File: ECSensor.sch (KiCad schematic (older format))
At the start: 8 parts, among them J2 EC_Sensor_Input_3_Pin, Q2 Q_PMOS_DSG

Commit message: schematic and pcb redesign
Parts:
- added FB3, FB4, FB5: Ferrite_Bead, Inductor_SMD:L_0402_1005Metric, symbol Device:Ferrite_Bead
- added R16, R17, R18: 0, Resistor_SMD:R_0402_1005Metric, symbol Device:R_Small_US
- C33: renamed from C26; footprint Capacitor_SMD:C_0603_1608Metric -> Capacitor_SMD:C_0402_1005Metric
- C34: renamed from C27; footprint Capacitor_SMD:C_0603_1608Metric -> Capacitor_SMD:C_0402_1005Metric
- C35: renamed from C28; footprint Capacitor_SMD:C_0603_1608Metric -> Capacitor_SMD:C_0402_1005Metric
- R13: renamed from R7; footprint Resistor_SMD:R_0603_1608Metric -> Resistor_SMD:R_0402_1005Metric
- R14: renamed from R8; footprint Resistor_SMD:R_0603_1608Metric -> Resistor_SMD:R_0402_1005Metric
- R15: renamed from R9; footprint Resistor_SMD:R_0603_1608Metric -> Resistor_SMD:R_0402_1005Metric
- renumbered J2 to J3
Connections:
- net CE: now also FB3.2, R16.2; no longer J3.1 (Pin_1)
- net RE: now also FB5.2, R18.2; no longer J3.3 (Pin_3)
- net WE: now also FB4.2, R17.2; no longer J3.2 (Pin_2)
- new net: FB3.1, J3.1 (Pin_1), R16.1
- new net: FB4.1, J3.2 (Pin_2), R17.1
- new net: FB5.1, J3.3 (Pin_3), R18.1
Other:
- moved on the sheet: C36, C37, C38, J4

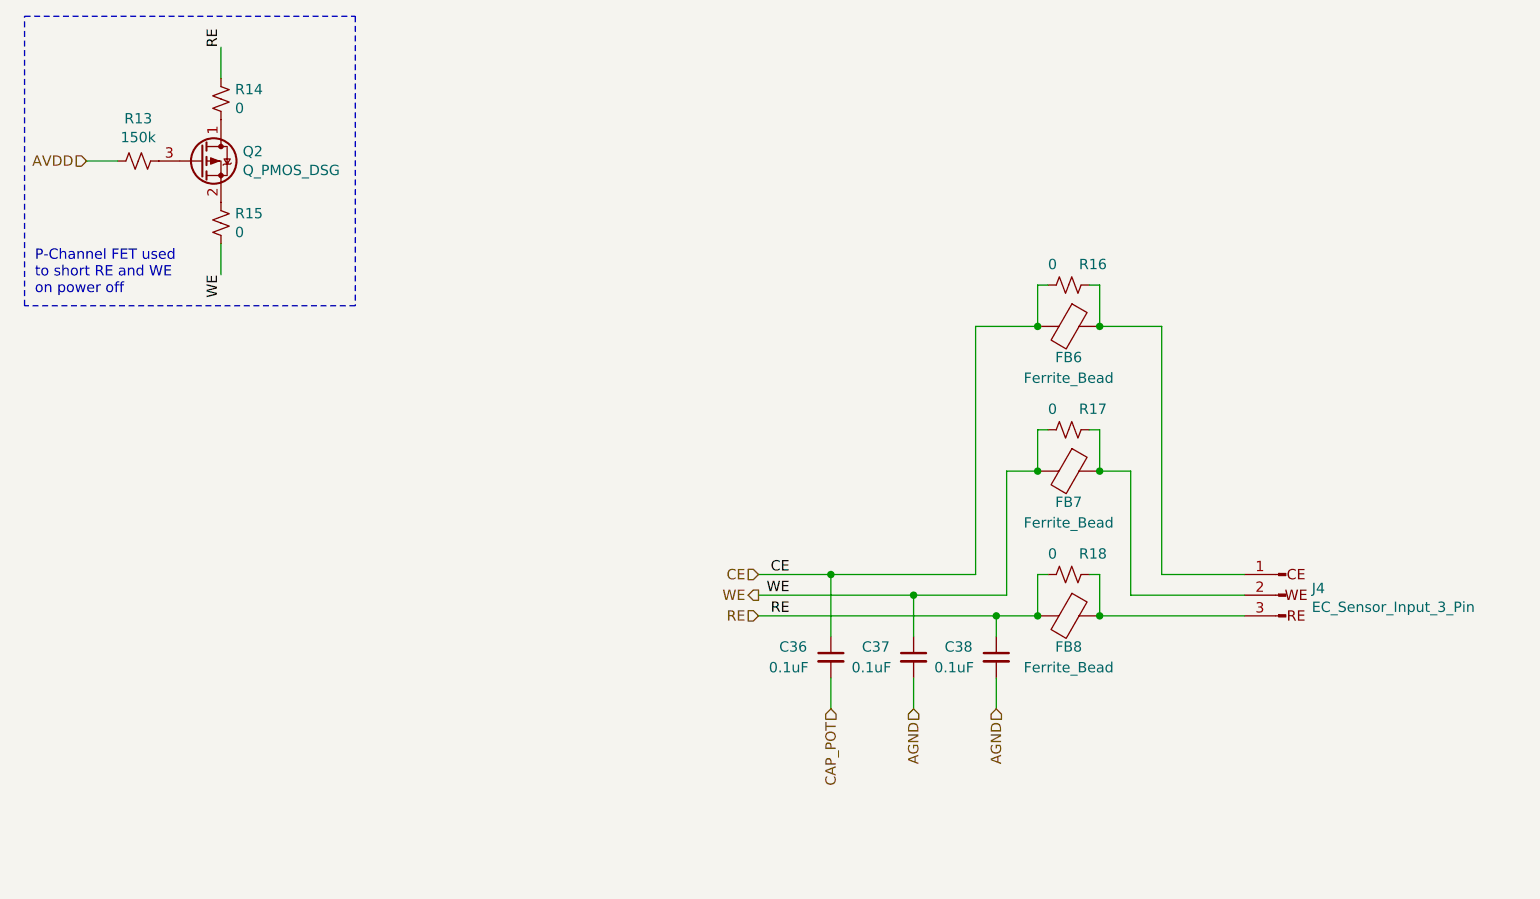
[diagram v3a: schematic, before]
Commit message: finsihed traces for one EC sensor
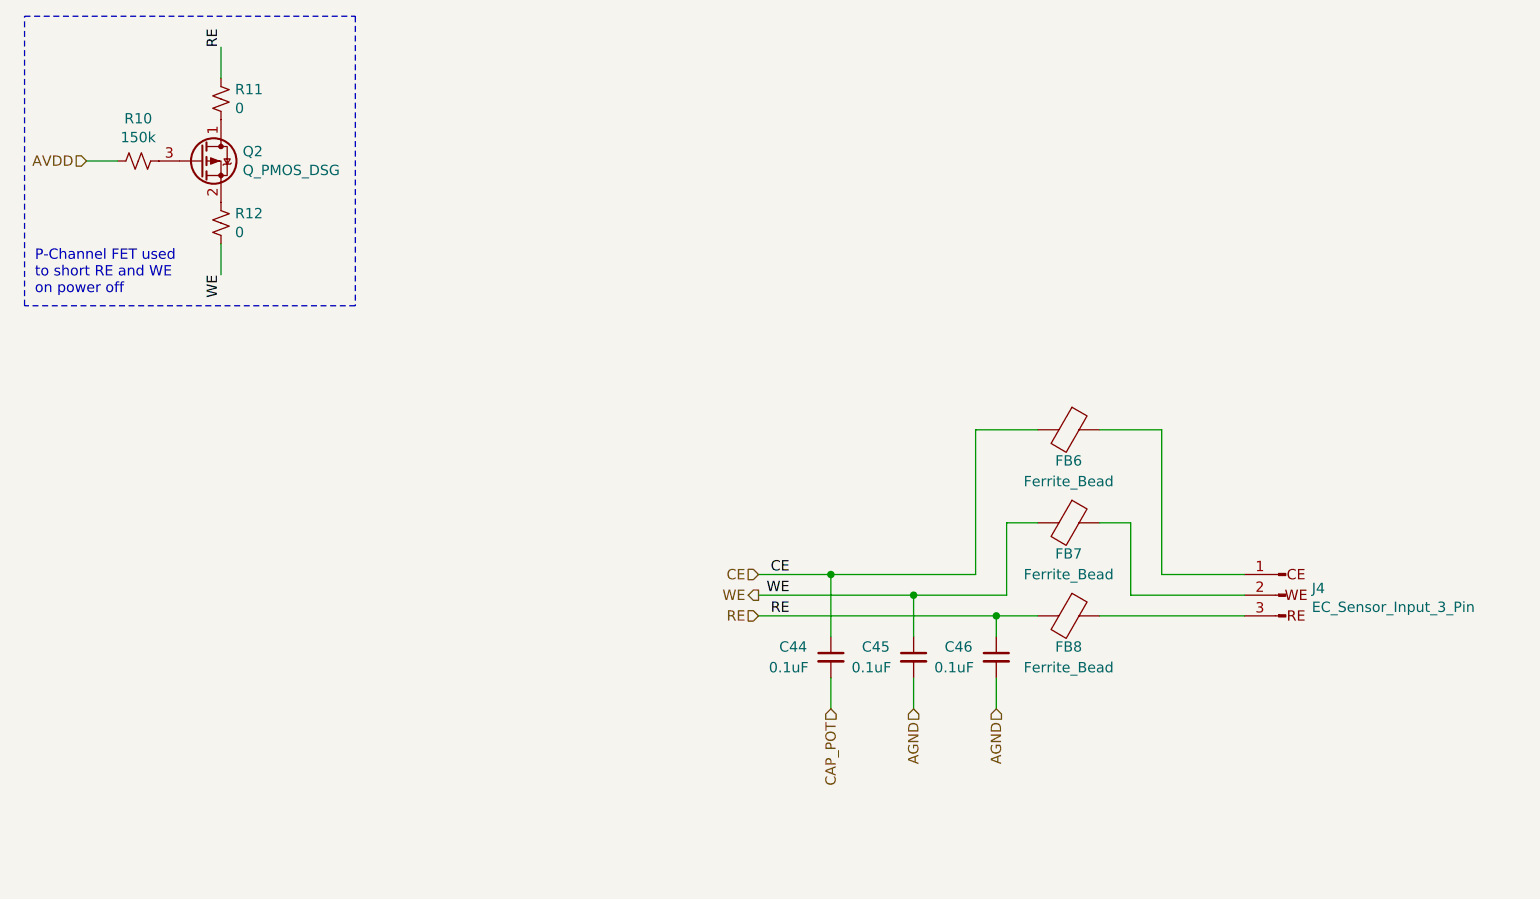
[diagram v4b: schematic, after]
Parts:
- removed R16, R17, R18: 0, Resistor_SMD:R_0402_1005Metric, symbol Device:R_Small_US
- renumbered C33 to C44, C34 to C45, C35 to C46, FB3 to FB6, FB4 to FB7, FB5 to FB8, J3 to J4, Q2 to Q1, R13 to R7, R14 to R8, R15 to R9
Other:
- moved on the sheet: FB6, FB7
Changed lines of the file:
@@
 $Descr A4 11693 8268
 encoding utf-8
-Sheet 2 5
+Sheet 5 5
 Title "ADuCM355 Template"
 Date ""
@@
 $EndDescr
 $Comp
-L Device:C_Small C34
+L Device:C_Small C45
 U 1 1 5DF76279
 P 5000 3750
-AR Path="/5DF7340A/5DF76279" Ref="C34"  Part="1"
-AR Path="/5DF54D0C/5DF76279" Ref="C37"  Part="1"
-F 0 "C37" H 4750 3800 50  0000 L CNN
+AR Path="/5DF7340A/5DF76279" Ref="C45"  Part="1"
+AR Path="/5DF54D0C/5DF76279" Ref="C34"  Part="1"
+F 0 "C45" H 4750 3800 50  0000 L CNN
 F 1 "0.1uF" H 4700 3700 50  0000 L CNN
 F 2 "Capacitor_SMD:C_0402_1005Metric" H 5000 3750 50  0001 C CNN
@@
 $EndComp
 $Comp
-L Device:C_Small C33
+L Device:C_Small C44
 U 1 1 5DF76497
 P 4600 3750
-AR Path="/5DF7340A/5DF76497" Ref="C33"  Part="1"
-AR Path="/5DF54D0C/5DF76497" Ref="C36"  Part="1"
-F 0 "C36" H 4350 3800 50  0000 L CNN
+AR Path="/5DF7340A/5DF76497" Ref="C44"  Part="1"
+AR Path="/5DF54D0C/5DF76497" Ref="C33"  Part="1"
+F 0 "C44" H 4350 3800 50  0000 L CNN
 F 1 "0.1uF" H 4300 3700 50  0000 L CNN
 F 2 "Capacitor_SMD:C_0402_1005Metric" H 4600 3750 50  0001 C CNN
@@
 $EndComp
 $Comp
-L Device:C_Small C35
+L Device:C_Small C46
 U 1 1 5DF768A0
 P 5400 3750
-AR Path="/5DF7340A/5DF768A0" Ref="C35"  Part="1"
-AR Path="/5DF54D0C/5DF768A0" Ref="C38"  Part="1"
-F 0 "C38" H 5150 3800 50  0000 L CNN
+AR Path="/5DF7340A/5DF768A0" Ref="C46"  Part="1"
+AR Path="/5DF54D0C/5DF768A0" Ref="C35"  Part="1"
+F 0 "C46" H 5150 3800 50  0000 L CNN
 F 1 "0.1uF" H 5100 3700 50  0000 L CNN
 F 2 "Capacitor_SMD:C_0402_1005Metric" H 5400 3750 50  0001 C CNN
@@
 $EndComp
 $Comp
-L SIB_Footprint:EC_Sensor_Input_3_Pin J3
+L SIB_Footprint:EC_Sensor_Input_3_Pin J4
 U 1 1 5DF7EEA4
 P 6800 3450
-AR Path="/5DF7340A/5DF7EEA4" Ref="J3"  Part="1"
-AR Path="/5DF54D0C/5DF7EEA4" Ref="J4"  Part="1"
+AR Path="/5DF7340A/5DF7EEA4" Ref="J4"  Part="1"
+AR Path="/5DF54D0C/5DF7EEA4" Ref="J3"  Part="1"
 F 0 "J4" H 6674 3483 50  0000 R CNN
 F 1 "EC_Sensor_Input_3_Pin" H 6674 3392 50  0000 R CNN
@@
 CE
 $Comp
-L Device:Q_PMOS_DSG Q2
+L Device:Q_PMOS_DSG Q1
 U 1 1 5E0080C3
 P 1550 1350
-AR Path="/5DF54D0C/5E0080C3" Ref="Q2"  Part="1"
-AR Path="/5DF7340A/5E0080C3" Ref="Q1"  Part="1"
+AR Path="/5DF54D0C/5E0080C3" Ref="Q1"  Part="1"
+AR Path="/5DF7340A/5E0080C3" Ref="Q2"  Part="1"
 F 0 "Q2" H 1755 1396 50  0000 L CNN
 F 1 "Q_PMOS_DSG" H 1755 1305 50  0000 L CNN
@@
 $EndComp
 $Comp
-L Device:R_Small_US R13
+L Device:R_Small_US R7
 U 1 1 5E00BDC0
 P 1250 1350
-AR Path="/5DF54D0C/5E00BDC0" Ref="R13"  Part="1"
-AR Path="/5DF7340A/5E00BDC0" Ref="R7"  Part="1"
-F 0 "R13" V 1045 1350 50  0000 C CNN
+AR Path="/5DF54D0C/5E00BDC0" Ref="R7"  Part="1"
+AR Path="/5DF7340A/5E00BDC0" Ref="R10"  Part="1"
+F 0 "R10" V 1045 1350 50  0000 C CNN
 F 1 "150k" V 1136 1350 50  0000 C CNN
 F 2 "Resistor_SMD:R_0402_1005Metric" H 1250 1350 50  0001 C CNN
@@
 $EndComp
 $Comp
-L Device:R_Small_US R14
+L Device:R_Small_US R8
 U 1 1 5E00C4B8
 P 1650 1050
-AR Path="/5DF54D0C/5E00C4B8" Ref="R14"  Part="1"
-AR Path="/5DF7340A/5E00C4B8" Ref="R8"  Part="1"
-F 0 "R14" H 1582 1004 50  0000 R CNN
+AR Path="/5DF54D0C/5E00C4B8" Ref="R8"  Part="1"
+AR Path="/5DF7340A/5E00C4B8" Ref="R11"  Part="1"
+F 0 "R11" H 1582 1004 50  0000 R CNN
 F 1 "0" H 1582 1095 50  0000 R CNN
 F 2 "Resistor_SMD:R_0402_1005Metric" H 1650 1050 50  0001 C CNN
@@
 $EndComp
 $Comp
-L Device:R_Small_US R15
+L Device:R_Small_US R9
 U 1 1 5E00C73E
 P 1650 1650
-AR Path="/5DF54D0C/5E00C73E" Ref="R15"  Part="1"
-AR Path="/5DF7340A/5E00C73E" Ref="R9"  Part="1"
-F 0 "R15" H 1718 1696 50  0000 L CNN
+AR Path="/5DF54D0C/5E00C73E" Ref="R9"  Part="1"
+AR Path="/5DF7340A/5E00C73E" Ref="R12"  Part="1"
+F 0 "R12" H 1718 1696 50  0000 L CNN
 F 1 "0" H 1718 1605 50  0000 L CNN
 F 2 "Resistor_SMD:R_0402_1005Metric" H 1650 1650 50  0001 C CNN
@@
 P-Channel FET used \nto short RE and WE\non power off
 Wire Wire Line
-	5900 2150 5900 1950
-Wire Wire Line
 	4600 4000 4600 3850
 Wire Wire Line
@@
 	6600 3450 6050 3450
 Wire Wire Line
-	6050 3450 6050 2850
+	6050 3450 6050 3100
 Wire Wire Line
 	6600 3350 6200 3350
 Wire Wire Line
-	6200 3350 6200 2150
-Wire Wire Line
-	6200 2150 5900 2150
-Wire Wire Line
-	5600 2150 5600 1950
-Wire Wire Line
-	5450 2850 5450 3450
-Wire Wire Line
-	5600 2150 5300 2150
-Wire Wire Line
-	5300 2150 5300 3350
+	6200 3350 6200 2650
+Wire Wire Line
+	6200 2650 5900 2650
+Wire Wire Line
+	5450 3100 5450 3450
+Wire Wire Line
+	5600 2650 5300 2650
+Wire Wire Line
+	5300 2650 5300 3350
 Text Label 4400 3350 2    50   ~ 0
 CE
@@
 Wire Wire Line
 	5400 3650 5400 3550
-Connection ~ 5600 2150
-Connection ~ 5900 2150
-Wire Wire Line
-	5850 1950 5900 1950
-Wire Wire Line
-	5650 1950 5600 1950
-$Comp
-L Device:R_Small_US R16
-U 1 1 6050AA87
-P 5750 1950
-AR Path="/5DF54D0C/6050AA87" Ref="R16"  Part="1"
-AR Path="/5DF7340A/6050AA87" Ref="R10"  Part="1"
-F 0 "R16" V 5650 2000 50  0000 L CNN
-F 1 "0" V 5650 1850 50  0000 L CNN
-F 2 "Resistor_SMD:R_0402_1005Metric" H 5750 1950 50  0001 C CNN
-F 3 "~" H 5750 1950 50  0001 C CNN
-	1    5750 1950
-	0    1    1    0
-$EndComp
-$Comp
-L Device:Ferrite_Bead FB3
+$Comp
+L Device:Ferrite_Bead FB6
 U 1 1 605069B7
-P 5750 2150
-AR Path="/5DF7340A/605069B7" Ref="FB3"  Part="1"
-AR Path="/5DF54D0C/605069B7" Ref="FB6"  Part="1"
-F 0 "FB6" V 5900 2150 50  0000 C CNN
-F 1 "Ferrite_Bead" V 6000 2150 50  0000 C CNN
-F 2 "Inductor_SMD:L_0402_1005Metric" V 5680 2150 50  0001 C CNN
-F 3 "~" H 5750 2150 50  0001 C CNN
-	1    5750 2150
-	0    1    1    0
-$EndComp
-$Comp
-L Device:R_Small_US R17
-U 1 1 60542D4E
 P 5750 2650
-AR Path="/5DF54D0C/60542D4E" Ref="R17"  Part="1"
-AR Path="/5DF7340A/60542D4E" Ref="R11"  Part="1"
-F 0 "R17" V 5650 2700 50  0000 L CNN
-F 1 "0" V 5650 2550 50  0000 L CNN
-F 2 "Resistor_SMD:R_0402_1005Metric" H 5750 2650 50  0001 C CNN
+AR Path="/5DF7340A/605069B7" Ref="FB6"  Part="1"
+AR Path="/5DF54D0C/605069B7" Ref="FB3"  Part="1"
+F 0 "FB6" V 5900 2650 50  0000 C CNN
+F 1 "Ferrite_Bead" V 6000 2650 50  0000 C CNN
+F 2 "Inductor_SMD:L_0402_1005Metric" V 5680 2650 50  0001 C CNN
 F 3 "~" H 5750 2650 50  0001 C CNN
 	1    5750 2650
@@
 $EndComp
 $Comp
-L Device:Ferrite_Bead FB4
+L Device:Ferrite_Bead FB7
 U 1 1 60542E8C
-P 5750 2850
-AR Path="/5DF7340A/60542E8C" Ref="FB4"  Part="1"
-AR Path="/5DF54D0C/60542E8C" Ref="FB7"  Part="1"
-F 0 "FB7" V 5900 2850 50  0000 C CNN
-F 1 "Ferrite_Bead" V 6000 2850 50  0000 C CNN
-F 2 "Inductor_SMD:L_0402_1005Metric" V 5680 2850 50  0001 C CNN
-F 3 "~" H 5750 2850 50  0001 C CNN
-	1    5750 2850
-	0    1    1    0
-$EndComp
-$Comp
-L Device:R_Small_US R18
-U 1 1 605441B7
-P 5750 3350
-AR Path="/5DF54D0C/605441B7" Ref="R18"  Part="1"
-AR Path="/5DF7340A/605441B7" Ref="R12"  Part="1"
-F 0 "R18" V 5650 3400 50  0000 L CNN
-F 1 "0" V 5650 3250 50  0000 L CNN
-F 2 "Resistor_SMD:R_0402_1005Metric" H 5750 3350 50  0001 C CNN
-F 3 "~" H 5750 3350 50  0001 C CNN
-	1    5750 3350
-	0    1    1    0
-$EndComp
-$Comp
-L Device:Ferrite_Bead FB5
+P 5750 3100
+AR Path="/5DF7340A/60542E8C" Ref="FB7"  Part="1"
+AR Path="/5DF54D0C/60542E8C" Ref="FB4"  Part="1"
+F 0 "FB7" V 5900 3100 50  0000 C CNN
+F 1 "Ferrite_Bead" V 6000 3100 50  0000 C CNN
+F 2 "Inductor_SMD:L_0402_1005Metric" V 5680 3100 50  0001 C CNN
+F 3 "~" H 5750 3100 50  0001 C CNN
+	1    5750 3100
+	0    1    1    0
+$EndComp
+$Comp
+L Device:Ferrite_Bead FB8
 U 1 1 6054431B
 P 5750 3550
-AR Path="/5DF7340A/6054431B" Ref="FB5"  Part="1"
-AR Path="/5DF54D0C/6054431B" Ref="FB8"  Part="1"
+AR Path="/5DF7340A/6054431B" Ref="FB8"  Part="1"
+AR Path="/5DF54D0C/6054431B" Ref="FB5"  Part="1"
 F 0 "FB8" V 5900 3550 50  0000 C CNN
 F 1 "Ferrite_Bead" V 6000 3550 50  0000 C CNN
@@
 $EndComp
 Wire Wire Line
-	6050 2850 5900 2850
-Wire Wire Line
-	5600 2850 5450 2850
+	6050 3100 5900 3100
+Wire Wire Line
+	5600 3100 5450 3100
 Wire Wire Line
 	5600 3550 5400 3550
@@
 	5900 3550 6600 3550
 Wire Wire Line
-	5850 3350 5900 3350
-Wire Wire Line
-	5900 3350 5900 3550
-Connection ~ 5900 3550
-Wire Wire Line
-	5650 3350 5600 3350
-Wire Wire Line
-	5600 3350 5600 3550
-Connection ~ 5600 3550
-Wire Wire Line
-	5650 2650 5600 2650
-Wire Wire Line
-	5600 2650 5600 2850
-Connection ~ 5600 2850
-Wire Wire Line
-	5850 2650 5900 2650
-Wire Wire Line
-	5900 2650 5900 2850
-Connection ~ 5900 2850
-Wire Wire Line
 	4250 3350 4600 3350
